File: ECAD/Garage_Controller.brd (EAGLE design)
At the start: 127 x 92.7 mm, 91 parts, among them IC1 LM358D, IC2 LM358D, J1 1885410000, J2 1885410000, J3 1885430000, J4 1885430000, J5 1885430000, J6 1885430000, J7 1885430000, Q1 35A/25V/8.5mΩ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

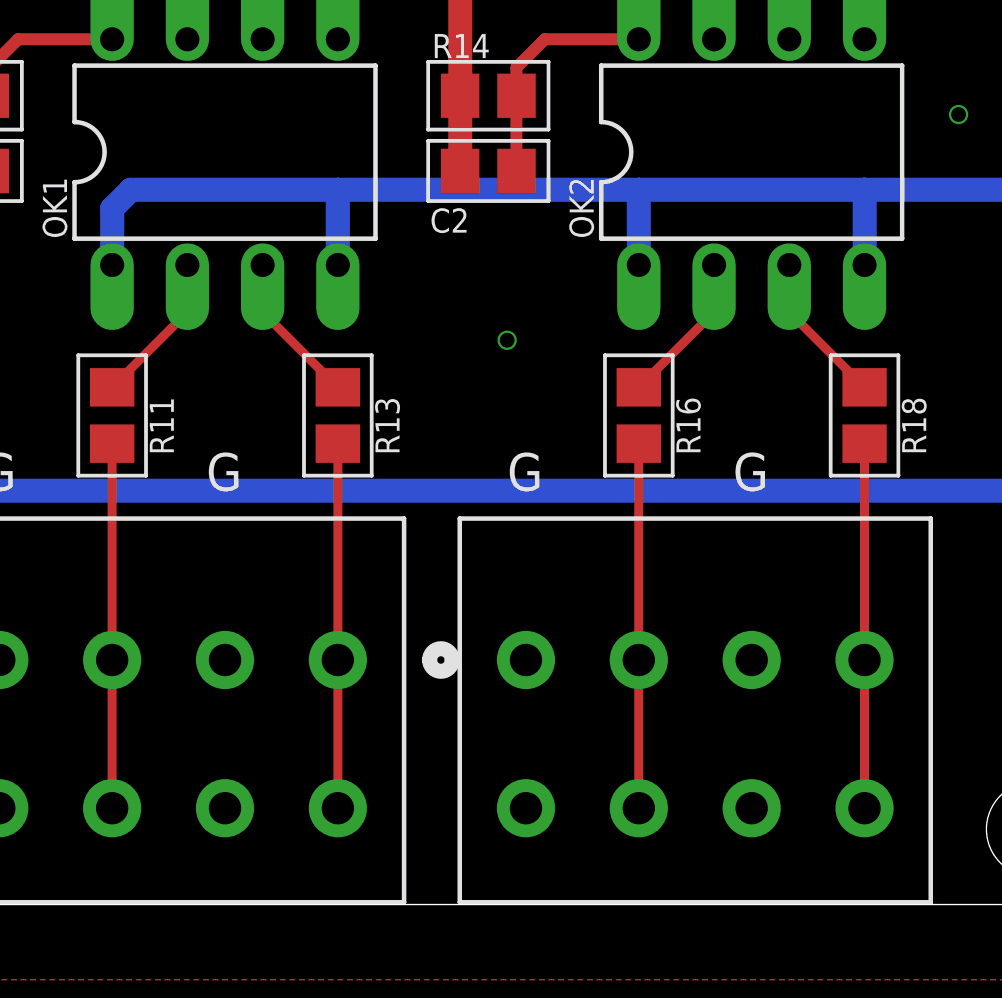
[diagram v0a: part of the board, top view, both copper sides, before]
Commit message: Providing +5V at DI connector
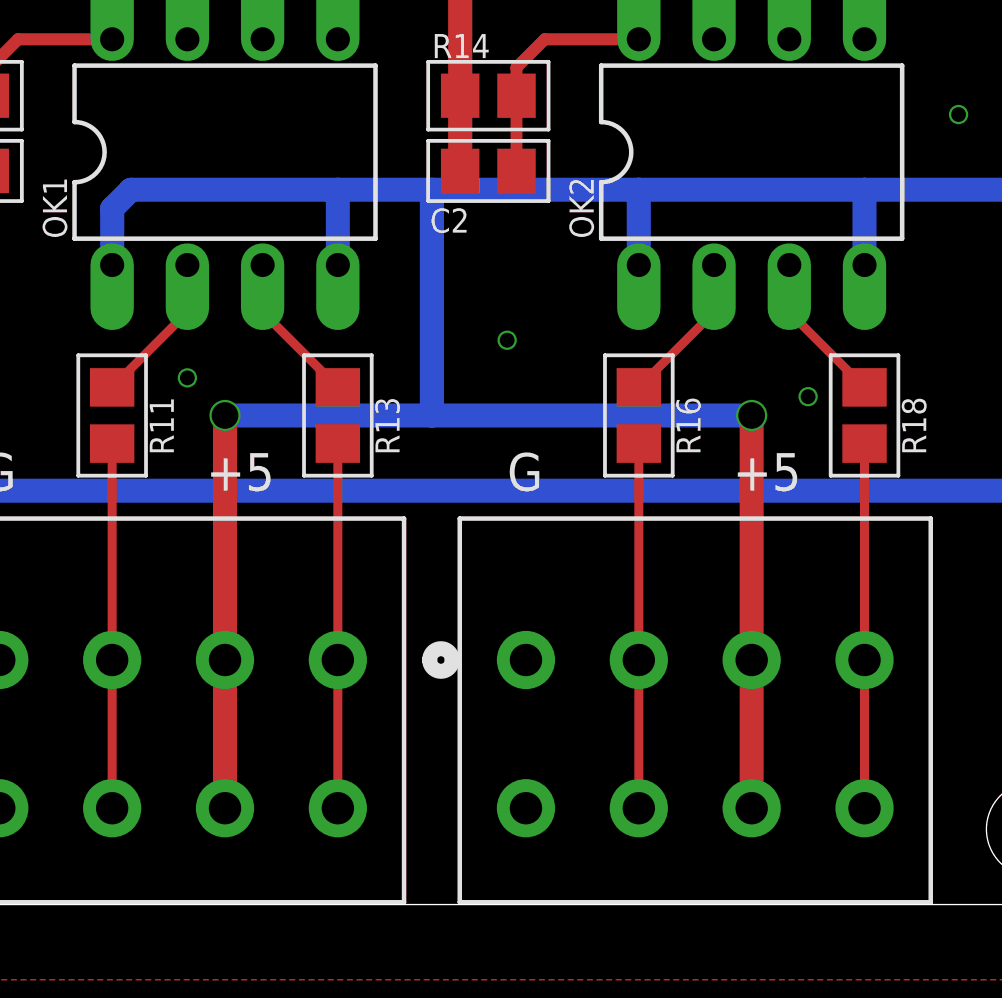
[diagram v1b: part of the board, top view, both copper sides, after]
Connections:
- net +5V/1: now also J4.5, J4.6, J5.5, J5.6
- net GND: no longer J4.5, J4.6, J5.5, J5.6
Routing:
- net +5V/1: track 71.3 -> 123.2 mm, vias 1 -> 3
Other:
- board text added: "+5"
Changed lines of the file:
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@@
 <text x="11.43" y="13.97" size="1.27" layer="21" font="fixed">+12</text>
 <text x="48.26" y="13.97" size="1.27" layer="21" font="fixed">G</text>
-<text x="55.88" y="13.97" size="1.27" layer="21" font="fixed">G</text>
+<text x="55.88" y="13.97" size="1.27" layer="21" font="fixed">+5</text>
 <text x="66.04" y="13.97" size="1.27" layer="21" font="fixed">G</text>
-<text x="73.66" y="13.97" size="1.27" layer="21" font="fixed">G</text>
+<text x="73.66" y="13.97" size="1.27" layer="21" font="fixed">+5</text>
 <text x="88.9" y="13.97" size="1.27" layer="21" font="fixed">G</text>
 <text x="96.52" y="13.97" size="1.27" layer="21" font="fixed">G</text>
@@
 <contactref element="J4" pad="1"/>
 <contactref element="J4" pad="2"/>
-<contactref element="J4" pad="5"/>
-<contactref element="J4" pad="6"/>
 <contactref element="J5" pad="1"/>
 <contactref element="J5" pad="2"/>
-<contactref element="J5" pad="5"/>
-<contactref element="J5" pad="6"/>
 <contactref element="C4" pad="2"/>
 <contactref element="J7" pad="1"/>
@@
 <via x="40.64" y="50.8" extent="1-16" drill="0.5"/>
 <via x="107.95" y="48.26" extent="1-16" drill="0.5"/>
+<via x="55.245" y="17.78" extent="1-16" drill="0.5"/>
+<via x="76.2" y="17.145" extent="1-16" drill="0.5"/>
 </signal>
 <signal name="+5V">
@@
 <wire x1="52.705" y1="23.495" x2="53.34" y2="24.13" width="0.8128" layer="16"/>
 <wire x1="53.34" y1="24.13" x2="60.325" y2="24.13" width="0.8128" layer="16"/>
-<wire x1="60.325" y1="24.13" x2="70.485" y2="24.13" width="0.8128" layer="16"/>
+<wire x1="60.325" y1="24.13" x2="63.5" y2="24.13" width="0.8128" layer="16"/>
+<wire x1="63.5" y1="24.13" x2="70.485" y2="24.13" width="0.8128" layer="16"/>
 <wire x1="70.485" y1="24.13" x2="78.105" y2="24.13" width="0.8128" layer="16"/>
 <wire x1="78.105" y1="24.13" x2="83.82" y2="24.13" width="0.8128" layer="16"/>
@@
 <contactref element="R38" pad="2"/>
 <wire x1="94.935" y1="33.655" x2="94.935" y2="36.195" width="0.3048" layer="1"/>
+<contactref element="J4" pad="5"/>
+<contactref element="J4" pad="6"/>
+<contactref element="J5" pad="5"/>
+<contactref element="J5" pad="6"/>
+<wire x1="63.5" y1="24.13" x2="63.5" y2="16.51" width="0.8128" layer="16"/>
+<wire x1="63.5" y1="16.51" x2="56.515" y2="16.51" width="0.8128" layer="16"/>
+<via x="56.515" y="16.51" extent="1-16" drill="0.9"/>
+<wire x1="56.515" y1="16.51" x2="56.515" y2="8.255" width="0.8128" layer="1"/>
+<wire x1="63.5" y1="16.51" x2="74.295" y2="16.51" width="0.8128" layer="16"/>
+<via x="74.295" y="16.51" extent="1-16" drill="0.9"/>
+<wire x1="74.295" y1="16.51" x2="74.295" y2="8.255" width="0.8128" layer="1"/>
+<wire x1="74.295" y1="8.255" x2="74.295" y2="3.2512" width="0.8128" layer="1"/>
+<wire x1="56.515" y1="8.255" x2="56.515" y2="3.2512" width="0.8128" layer="1"/>
 </signal>
 <signal name="DAC0">

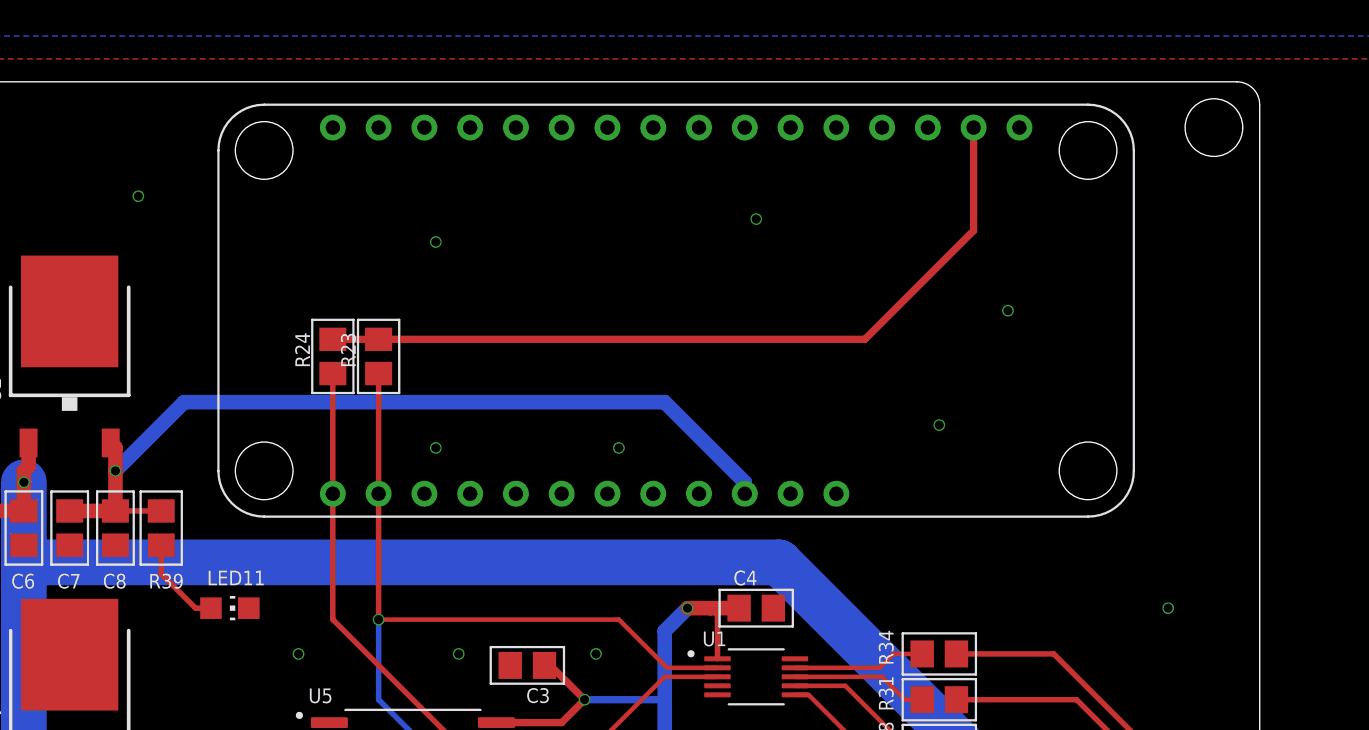
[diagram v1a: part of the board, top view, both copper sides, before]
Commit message: Switching to Huzzah ESP8266 breakout
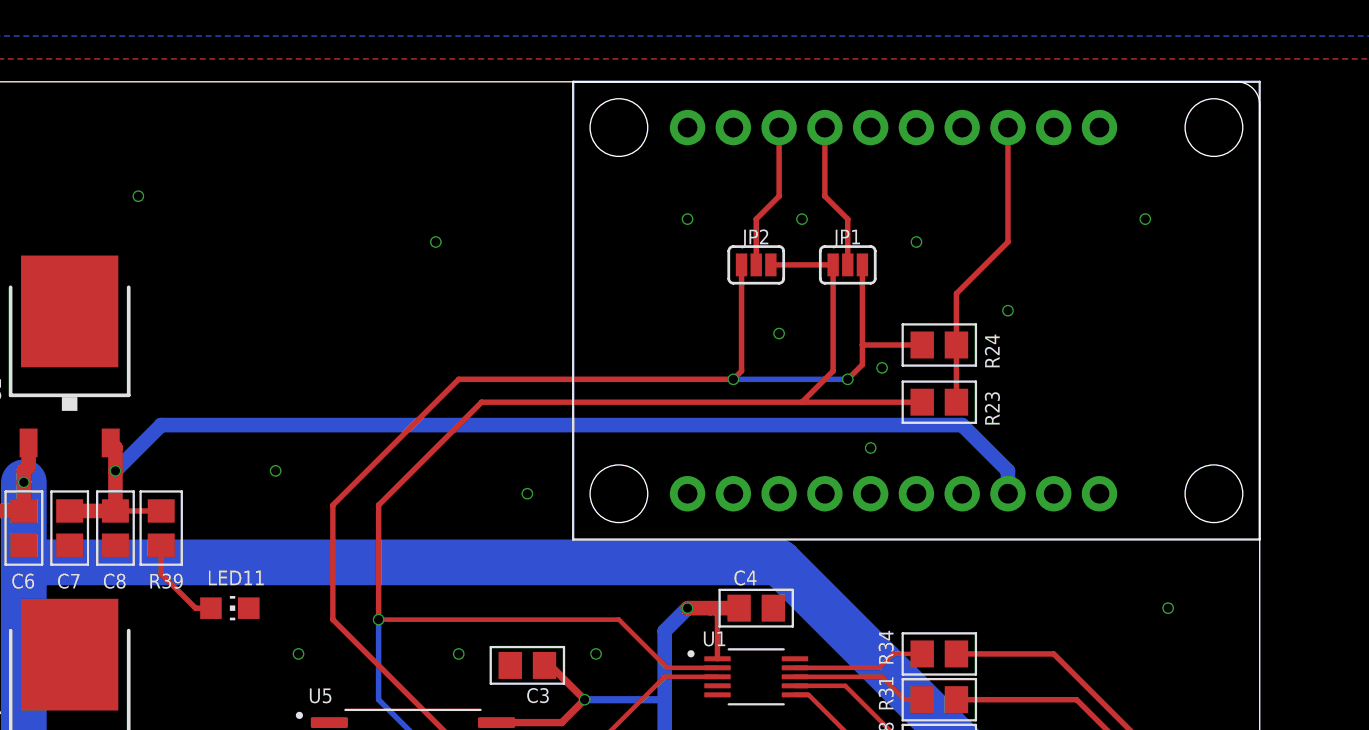
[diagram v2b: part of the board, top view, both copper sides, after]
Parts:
- removed U$1: ADAFRUIT_HUZZAH32, FRC696:FEATHER
- added JP1, JP2: JUMPER-SMT_3_1-NC_PASTE_SILK, SparkFun-Jumpers:SMT-JUMPER_3_1-NC_PASTE_SILK
- added U$2: HUZZAH_ESP8266_BREAKOUT, adafruit:HUZZAH_ESP8266_BREAKOUT
- moved R24 33.7 mm to (58.4, 78.1), turned to 0 degrees
- moved R23 31.2 mm to (58.4, 74.9), turned to 0 degrees
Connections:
- new net N$39: JP2.2, U$2.18
- new net N$40: JP1.2, U$2.17
- new net VBAT: U$2.9
- net +5V: now also U$2.8; no longer U$1.26
- net GND: now also U$2.10, U$2.11; no longer U$1.4
- net N$35: now also U$2.13; no longer U$1.2
- net SCL: now also JP1.1, JP2.3; no longer U$1.18
- net SDA: now also JP1.3, JP2.1; no longer U$1.17
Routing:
- net SDA: track 39.5 -> 80.2 mm, vias 0 -> 2
- net SCL: track 46.1 -> 83.2 mm
- net N$35: track 43.8 -> 16.4 mm
- net +5V: track 47.9 -> 61.9 mm
- net N$40: track 0.00 -> 8.15 mm
- net N$39: track 0.00 -> 8.15 mm
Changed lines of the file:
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@@
 <wire x1="78.74" y1="50.8" x2="125.73" y2="50.8" width="0" layer="20"/>
 <wire x1="125.73" y1="50.8" x2="127" y2="49.53" width="0" layer="20" curve="-90"/>
-<hole x="73.66" y="90.17" drill="3.2"/>
 <hole x="124.46" y="48.26" drill="3.2"/>
 <text x="11.43" y="13.97" size="1.27" layer="21" font="fixed">+12</text>
@@
 <attribute name="NAME" x="12.7" y="29.21" size="0.8128" layer="25" font="fixed" ratio="20" rot="R270" align="bottom-center"/>
 </element>
-<element name="U$1" library="FRC696" package="FEATHER" value="ADAFRUIT_HUZZAH32" x="69.215" y="91.44" smashed="yes" rot="R180"/>
 <element name="R1" library="resistor" package="R0805" value="1k" x="10.16" y="38.1" smashed="yes" rot="R270">
 <attribute name="NAME" x="11.43" y="38.735" size="0.8128" layer="25" font="fixed" rot="R270"/>
@@
 <attribute name="NAME" x="45.265" y="61.392" size="0.8128" layer="25" font="fixed"/>
 </element>
-<element name="R23" library="resistor" package="R0805" value="3.3k" x="27.305" y="77.47" smashed="yes" rot="R90">
-<attribute name="NAME" x="26.035" y="76.835" size="0.8128" layer="25" font="fixed" rot="R90"/>
-</element>
-<element name="R24" library="resistor" package="R0805" value="3.3k" x="24.765" y="77.47" smashed="yes" rot="R90">
-<attribute name="NAME" x="23.495" y="76.835" size="0.8128" layer="25" font="fixed" rot="R90"/>
+<element name="R23" library="resistor" package="R0805" value="3.3k" x="58.42" y="74.93" smashed="yes">
+<attribute name="NAME" x="60.96" y="75.565" size="0.8128" layer="25" font="fixed" rot="R270"/>
+</element>
+<element name="R24" library="resistor" package="R0805" value="3.3k" x="58.42" y="78.105" smashed="yes">
+<attribute name="NAME" x="60.96" y="78.74" size="0.8128" layer="25" font="fixed" rot="R270"/>
 </element>
 <element name="IC1" library="linear" package="SO08" value="LM358D" x="95.25" y="24.13" smashed="yes" rot="R90">
@@
 <attribute name="VALUE" x="17.78" y="60.96" size="1.27" layer="27"/>
 </element>
+<element name="U$2" library="adafruit" package="HUZZAH_ESP8266_BREAKOUT" value="HUZZAH_ESP8266_BREAKOUT" x="76.2" y="92.71" rot="R180"/>
+<element name="JP1" library="SparkFun-Jumpers" package="SMT-JUMPER_3_1-NC_PASTE_SILK" value="JUMPER-SMT_3_1-NC_PASTE_SILK" x="53.34" y="82.55" smashed="yes">
+<attribute name="NAME" x="53.34" y="83.693" size="0.8128" layer="25" font="fixed" ratio="20" align="bottom-center"/>
+</element>
+<element name="JP2" library="SparkFun-Jumpers" package="SMT-JUMPER_3_1-NC_PASTE_SILK" value="JUMPER-SMT_3_1-NC_PASTE_SILK" x="48.26" y="82.55" smashed="yes">
+<attribute name="NAME" x="48.26" y="83.693" size="0.8128" layer="25" font="fixed" ratio="20" align="bottom-center"/>
+</element>
 </elements>
 <signals>
 <signal name="GND">
-<contactref element="U$1" pad="4"/>
 <contactref element="Q1" pad="3"/>
 <contactref element="D1" pad="A"/>
@@
 <via x="2.54" y="81.28" extent="1-16" drill="0.5"/>
 <via x="30.48" y="83.82" extent="1-16" drill="0.5"/>
-<via x="48.26" y="85.09" extent="1-16" drill="0.5"/>
+<via x="44.45" y="85.09" extent="1-16" drill="0.5"/>
 <via x="62.23" y="80.01" extent="1-16" drill="0.5"/>
-<via x="58.42" y="73.66" extent="1-16" drill="0.5"/>
+<via x="54.61" y="72.39" extent="1-16" drill="0.5"/>
 <via x="39.37" y="60.96" extent="1-16" drill="0.5"/>
-<via x="40.64" y="72.39" extent="1-16" drill="0.5"/>
-<via x="30.48" y="72.39" extent="1-16" drill="0.5"/>
+<via x="35.56" y="69.85" extent="1-16" drill="0.5"/>
+<via x="21.59" y="71.12" extent="1-16" drill="0.5"/>
 <via x="35.56" y="36.83" extent="1-16" drill="0.5"/>
 <via x="38.1" y="43.18" extent="1-16" drill="0.5"/>
@@
 <via x="55.245" y="17.78" extent="1-16" drill="0.5"/>
 <via x="76.2" y="17.145" extent="1-16" drill="0.5"/>
+<contactref element="U$2" pad="11"/>
+<contactref element="U$2" pad="10"/>
+<via x="50.8" y="85.09" extent="1-16" drill="0.5"/>
+<via x="49.53" y="78.74" extent="1-16" drill="0.5"/>
+<via x="57.15" y="83.82" extent="1-16" drill="0.5"/>
+<via x="69.85" y="85.09" extent="1-16" drill="0.5"/>
+<via x="55.245" y="76.835" extent="1-16" drill="0.5"/>
 </signal>
 <signal name="+5V">
-<contactref element="U$1" pad="26"/>
 <contactref element="U2" pad="2"/>
 <contactref element="C7" pad="1"/>
 <contactref element="C8" pad="1"/>
-<wire x1="47.625" y1="69.85" x2="47.625" y2="70.485" width="0.8128" layer="16"/>
-<wire x1="47.625" y1="70.485" x2="43.18" y2="74.93" width="0.8128" layer="16"/>
-<wire x1="43.18" y1="74.93" x2="16.51" y2="74.93" width="0.8128" layer="16"/>
-<wire x1="16.51" y1="74.93" x2="12.7" y2="71.12" width="0.8128" layer="16"/>
 <via x="12.7" y="71.12" extent="1-16" drill="0.5"/>
 <wire x1="12.7" y1="71.12" x2="12.7" y2="72.41" width="0.8128" layer="1"/>
@@
 <contactref element="R39" pad="2"/>
 <wire x1="15.24" y1="68.895" x2="12.7" y2="68.895" width="0.3048" layer="1"/>
+<contactref element="U$2" pad="8"/>
+<wire x1="12.7" y1="71.12" x2="15.24" y2="73.66" width="0.8128" layer="16"/>
+<wire x1="15.24" y1="73.66" x2="59.69" y2="73.66" width="0.8128" layer="16"/>
+<wire x1="59.69" y1="73.66" x2="62.23" y2="71.12" width="0.8128" layer="16"/>
+<wire x1="62.23" y1="71.12" x2="62.23" y2="69.85" width="0.8128" layer="16"/>
 </signal>
 <signal name="N$1">
@@
 </signal>
 <signal name="SCL">
-<contactref element="U$1" pad="18"/>
 <contactref element="U1" pad="2"/>
 <contactref element="R23" pad="1"/>
-<wire x1="27.305" y1="76.52" x2="27.305" y2="69.85" width="0.3048" layer="1"/>
 <contactref element="U5" pad="14"/>
-<wire x1="27.305" y1="69.85" x2="27.305" y2="62.865" width="0.3048" layer="1"/>
 <via x="27.305" y="62.865" extent="1-16" drill="0.5"/>
 <wire x1="27.305" y1="62.865" x2="27.305" y2="58.42" width="0.3048" layer="16"/>
@@
 <wire x1="43.315" y1="60.19" x2="40.64" y2="62.865" width="0.254" layer="1"/>
 <wire x1="40.64" y1="62.865" x2="27.305" y2="62.865" width="0.254" layer="1"/>
+<contactref element="JP2" pad="3"/>
+<contactref element="JP1" pad="1"/>
+<wire x1="27.305" y1="62.865" x2="27.305" y2="69.215" width="0.3048" layer="1"/>
+<wire x1="27.305" y1="69.215" x2="33.02" y2="74.93" width="0.3048" layer="1"/>
+<wire x1="33.02" y1="74.93" x2="50.8" y2="74.93" width="0.3048" layer="1"/>
+<wire x1="50.8" y1="74.93" x2="52.5272" y2="76.6572" width="0.3048" layer="1"/>
+<wire x1="52.5272" y1="82.55" x2="52.5272" y2="76.6572" width="0.3048" layer="1"/>
+<wire x1="52.5272" y1="82.55" x2="49.0728" y2="82.55" width="0.3048" layer="1"/>
+<wire x1="50.8" y1="74.93" x2="57.47" y2="74.93" width="0.3048" layer="1"/>
 </signal>
 <signal name="SDA">
-<contactref element="U$1" pad="17"/>
 <contactref element="U1" pad="3"/>
 <contactref element="R24" pad="1"/>
-<wire x1="24.765" y1="76.52" x2="24.765" y2="69.85" width="0.3048" layer="1"/>
 <contactref element="U5" pad="15"/>
-<wire x1="24.765" y1="69.85" x2="24.765" y2="62.865" width="0.3048" layer="1"/>
 <wire x1="31.75" y1="55.88" x2="33.85" y2="55.88" width="0.3048" layer="1"/>
 <wire x1="46.11" y1="59.69" x2="43.18" y2="59.69" width="0.254" layer="1"/>
@@
 <wire x1="39.37" y1="55.88" x2="33.85" y2="55.88" width="0.254" layer="1"/>
 <wire x1="31.75" y1="55.88" x2="24.765" y2="62.865" width="0.3048" layer="1"/>
+<contactref element="JP1" pad="3"/>
+<contactref element="JP2" pad="1"/>
+<wire x1="24.765" y1="62.865" x2="24.765" y2="69.215" width="0.3048" layer="1"/>
+<wire x1="24.765" y1="69.215" x2="31.75" y2="76.2" width="0.3048" layer="1"/>
+<wire x1="31.75" y1="76.2" x2="46.99" y2="76.2" width="0.3048" layer="1"/>
+<wire x1="47.4472" y1="82.55" x2="47.4472" y2="76.6572" width="0.3048" layer="1"/>
+<wire x1="47.4472" y1="76.6572" x2="46.99" y2="76.2" width="0.3048" layer="1"/>
+<via x="46.99" y="76.2" extent="1-16" drill="0.5"/>
+<wire x1="46.99" y1="76.2" x2="53.34" y2="76.2" width="0.3048" layer="16"/>
+<wire x1="54.1528" y1="82.55" x2="54.1528" y2="78.105" width="0.3048" layer="1"/>
+<wire x1="54.1528" y1="78.105" x2="54.1528" y2="77.0128" width="0.3048" layer="1"/>
+<wire x1="54.1528" y1="77.0128" x2="53.34" y2="76.2" width="0.3048" layer="1"/>
+<via x="53.34" y="76.2" extent="1-16" drill="0.5"/>
+<wire x1="57.47" y1="78.105" x2="54.1528" y2="78.105" width="0.3048" layer="1"/>
 </signal>
 <signal name="K1">
@@
 </signal>
 <signal name="N$35">
-<contactref element="U$1" pad="2"/>
 <contactref element="R24" pad="2"/>
 <contactref element="R23" pad="2"/>
-<wire x1="60.325" y1="90.17" x2="60.325" y2="84.455" width="0.4064" layer="1"/>
-<wire x1="60.325" y1="84.455" x2="54.29" y2="78.42" width="0.4064" layer="1"/>
-<wire x1="27.305" y1="78.42" x2="27.94" y2="78.42" width="0.4064" layer="1"/>
-<wire x1="27.94" y1="78.42" x2="54.29" y2="78.42" width="0.4064" layer="1"/>
-<wire x1="24.765" y1="78.42" x2="27.305" y2="78.42" width="0.4064" layer="1"/>
+<contactref element="U$2" pad="13"/>
+<wire x1="59.37" y1="74.93" x2="59.37" y2="78.105" width="0.3048" layer="1"/>
+<wire x1="62.23" y1="90.17" x2="62.23" y2="83.82" width="0.3048" layer="1"/>
+<wire x1="62.23" y1="83.82" x2="59.37" y2="80.96" width="0.3048" layer="1"/>
+<wire x1="59.37" y1="78.105" x2="59.37" y2="80.96" width="0.3048" layer="1"/>
 </signal>
 <signal name="N$36">
@@
 <wire x1="15.24" y1="65.405" x2="15.24" y2="66.995" width="0.3048" layer="1"/>
 </signal>
+<signal name="VBAT">
+<contactref element="U$2" pad="9"/>
+</signal>
+<signal name="N$39">
+<contactref element="U$2" pad="18"/>
+<contactref element="JP2" pad="2"/>
+<wire x1="49.53" y1="90.17" x2="49.53" y2="86.36" width="0.3048" layer="1"/>
+<wire x1="49.53" y1="86.36" x2="48.26" y2="85.09" width="0.3048" layer="1"/>
+<wire x1="48.26" y1="85.09" x2="48.26" y2="82.55" width="0.3048" layer="1"/>
+</signal>
+<signal name="N$40">
+<contactref element="U$2" pad="17"/>
+<contactref element="JP1" pad="2"/>
+<wire x1="52.07" y1="90.17" x2="52.07" y2="86.36" width="0.3048" layer="1"/>
+<wire x1="52.07" y1="86.36" x2="53.34" y2="85.09" width="0.3048" layer="1"/>
+<wire x1="53.34" y1="85.09" x2="53.34" y2="82.55" width="0.3048" layer="1"/>
+</signal>
 </signals>
